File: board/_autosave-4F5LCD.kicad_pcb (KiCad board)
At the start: 2 copper layers, 58 parts, among them J101 Conn_01x10_Pin, J102 Conn_02x16_Top_Bottom, J103 Conn_02x02_Counter_Clockwise, U101 TLS850C2TEV33, U102 ESP32-S3-DEVKITC-1U-N8R2, U103 MCP2515-xSO, U104 SN65HVD230, U105 MCP2515-xSO, U106 SN65HVD230, U107 MCP2515-xSO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

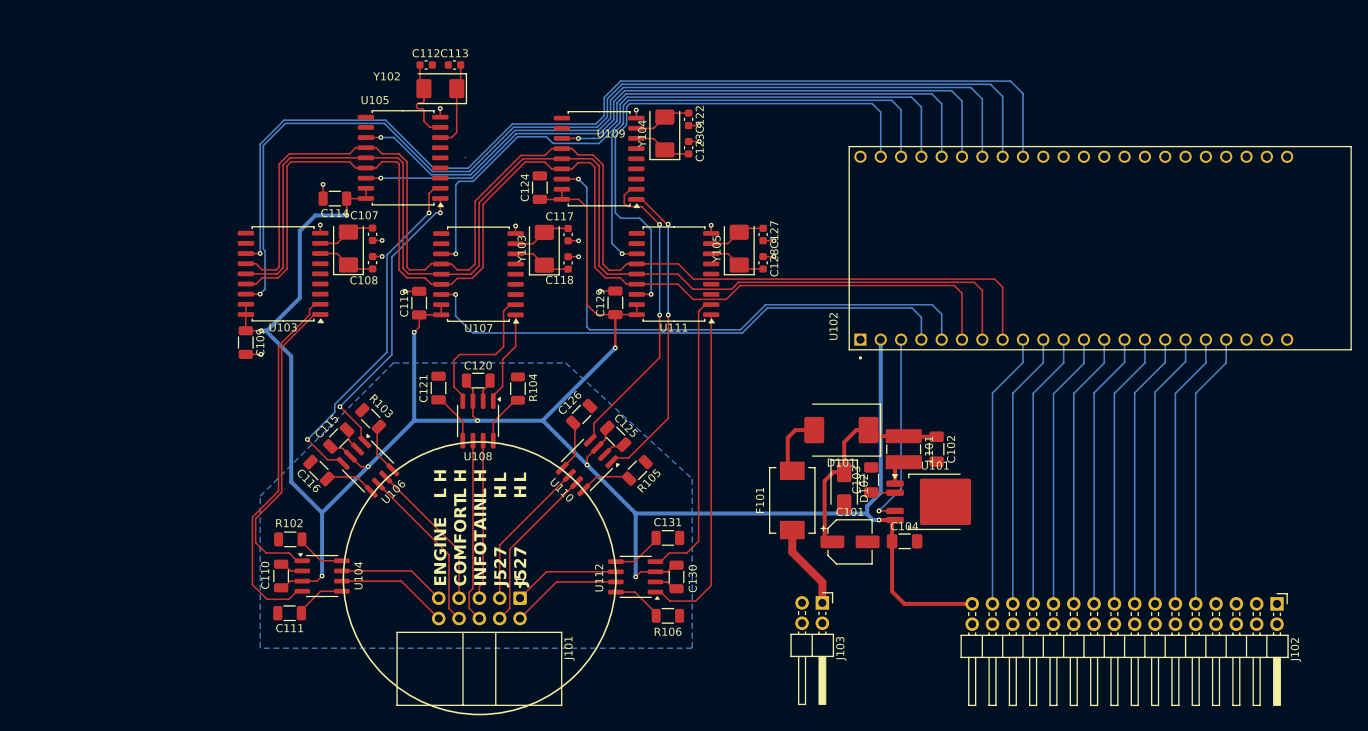
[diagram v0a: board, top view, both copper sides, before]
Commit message: Added stl and skp files for 3D printing, changed ground planes and net names, exported schematics as pdf
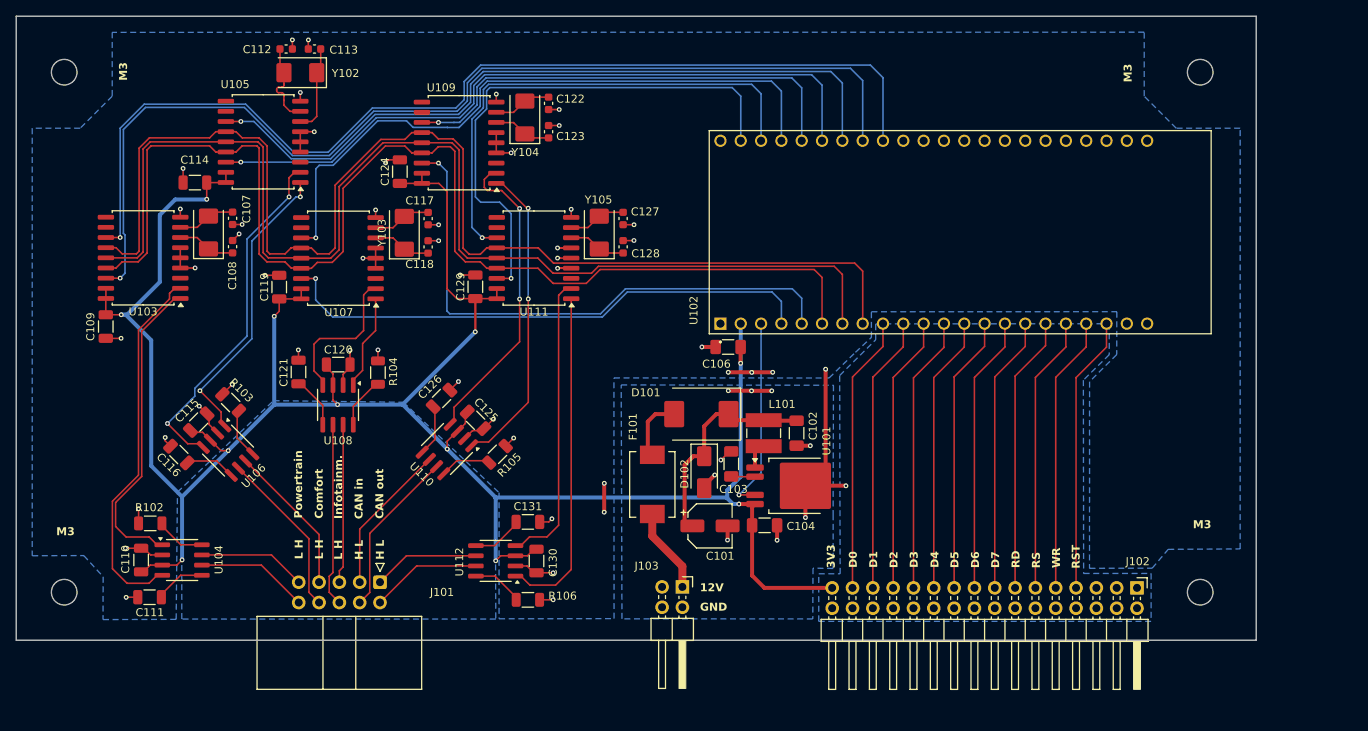
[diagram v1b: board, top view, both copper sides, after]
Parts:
- added C106: 100nF, Capacitor_SMD:C_1206_3216Metric_Pad1.33x1.80mm_HandSolder, F.Cu at (159.5, 89.3)
- added REF**: MountingHole_3.2mm_M3, MountingHole:MountingHole_3.2mm_M3, F.Cu at (76.5, 55.0)
- added REF**: MountingHole_3.2mm_M3, MountingHole:MountingHole_3.2mm_M3, F.Cu at (76.5, 120.0)
- added REF**: MountingHole_3.2mm_M3, MountingHole:MountingHole_3.2mm_M3, F.Cu at (218.5, 120.0)
- added REF**: MountingHole_3.2mm_M3, MountingHole:MountingHole_3.2mm_M3, F.Cu at (218.5, 55.0)
- J103: value Conn_02x02_Counter_Clockwise -> 02x02
- moved C117 17.6 mm to (122.0, 73.3)
- moved C118 17.6 mm to (122.0, 76.8)
- moved C124 17.6 mm to (118.5, 67.4)
- moved C126 17.6 mm to (123.7, 95.8)
- moved J101 17.6 mm to (116.0, 118.8)
- moved U108 17.6 mm to (110.7, 96.6)
- moved U109 17.6 mm to (125.9, 63.8)
- moved U110 17.6 mm to (124.3, 102.1)
- moved C123 17.6 mm to (137.0, 62.4)
- moved C101 17.6 mm to (157.2, 111.7)
- moved C102 17.6 mm to (168.1, 100.1)
- moved C103 17.6 mm to (159.9, 104.0)
- moved C104 17.6 mm to (164.1, 111.6)
- moved C107 17.6 mm to (97.5, 73.3)
- moved C108 17.6 mm to (97.5, 76.8)
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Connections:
- C101 pad 2: CAN_GND -> GND_PWR
- C102 pad 2: CAN_GND -> GND_PWR
- C103 pad 2: CAN_GND -> GND_PWR
- C104 pad 2: CAN_GND -> GND_PWR
- C107 pad 2: CAN_GND -> GND_MCU
- C108 pad 1: CAN_GND -> GND_MCU
- C109 pad 2: CAN_GND -> GND_MCU
- C110 pad 2: CAN_GND -> GND_MCU
- C111 pad 2: CAN_GND -> GND_MCU
- C112 pad 2: CAN_GND -> GND_MCU
- C113 pad 1: CAN_GND -> GND_MCU
- C114 pad 2: CAN_GND -> GND_MCU
- C115 pad 2: CAN_GND -> GND_MCU
- C116 pad 2: CAN_GND -> GND_MCU
- C117 pad 2: CAN_GND -> GND_MCU
- C118 pad 1: CAN_GND -> GND_MCU
- C119 pad 2: CAN_GND -> GND_MCU
- C120 pad 2: CAN_GND -> GND_MCU
- C121 pad 2: CAN_GND -> GND_MCU
- C122 pad 2: CAN_GND -> GND_MCU
- C123 pad 1: CAN_GND -> GND_MCU
- C124 pad 2: CAN_GND -> GND_MCU
- C125 pad 2: CAN_GND -> GND_MCU
- C126 pad 2: CAN_GND -> GND_MCU
- C127 pad 2: CAN_GND -> GND_MCU
- C128 pad 1: CAN_GND -> GND_MCU
- C129 pad 2: CAN_GND -> GND_MCU
- C130 pad 2: CAN_GND -> GND_MCU
- C131 pad 2: CAN_GND -> GND_MCU
- D102 pad 2: CAN_GND -> GND_PWR
- J102 pad 10: CAN_GND -> GND_LCD
- J102 pad 12: CAN_GND -> GND_LCD
- J102 pad 14: CAN_GND -> GND_LCD
- J102 pad 16: CAN_GND -> GND_LCD
- J102 pad 18: CAN_GND -> GND_LCD
- J102 pad 20: CAN_GND -> GND_LCD
- J102 pad 22: CAN_GND -> GND_LCD
- J102 pad 24: CAN_GND -> GND_LCD
- J102 pad 26: CAN_GND -> GND_LCD
- J102 pad 28: CAN_GND -> GND_LCD
- J102 pad 30: CAN_GND -> GND_LCD
- J102 pad 32: CAN_GND -> GND_LCD
- J102 pad 6: unconnected-(J102-Pin_6-Pad6) -> GND_LCD
- J102 pad 7: unconnected-(J102-Pin_7-Pad7) -> LCD_RST
- J102 pad 8: CAN_GND -> GND_LCD
- J103 pad 2: CAN_GND -> GND_PWR
- R102 pad 2: CAN_GND -> GND_MCU
- R103 pad 2: CAN_GND -> GND_MCU
- R104 pad 2: CAN_GND -> GND_MCU
- R105 pad 2: CAN_GND -> GND_MCU
- R106 pad 2: CAN_GND -> GND_MCU
- U101 pad 3: CAN_GND -> GND_PWR
- U102 pad J1_20: unconnected-(U102-GPIO14-PadJ1_20) -> LCD_RST
- U102 pad J1_22: CAN_GND -> GND_MCU
- U102 pad J3_1: CAN_GND -> GND_MCU
- U102 pad J3_21: CAN_GND -> GND_MCU
- U102 pad J3_22: CAN_GND -> GND_MCU
- U103 pad 4: CAN_GND -> GND_MCU
- U103 pad 5: CAN_GND -> GND_MCU
- U103 pad 6: CAN_GND -> GND_MCU
- U103 pad 9: CAN_GND -> GND_MCU
- U104 pad 2: CAN_GND -> GND_MCU
- U105 pad 4: CAN_GND -> GND_MCU
- U105 pad 5: CAN_GND -> GND_MCU
- U105 pad 6: CAN_GND -> GND_MCU
- U105 pad 9: CAN_GND -> GND_MCU
- U106 pad 2: CAN_GND -> GND_MCU
- U107 pad 4: CAN_GND -> GND_MCU
- U107 pad 5: CAN_GND -> GND_MCU
- U107 pad 6: CAN_GND -> GND_MCU
- U107 pad 9: CAN_GND -> GND_MCU
- U108 pad 2: CAN_GND -> GND_MCU
- U109 pad 4: CAN_GND -> GND_MCU
- U109 pad 5: CAN_GND -> GND_MCU
- U109 pad 6: CAN_GND -> GND_MCU
- U109 pad 9: CAN_GND -> GND_MCU
- U110 pad 2: CAN_GND -> GND_MCU
- U111 pad 4: CAN_GND -> GND_MCU
- U111 pad 5: CAN_GND -> GND_MCU
- U111 pad 6: CAN_GND -> GND_MCU
- U111 pad 9: CAN_GND -> GND_MCU
- U112 pad 2: CAN_GND -> GND_MCU
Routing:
- net GND_MCU: track 0.00 -> 101.3 mm, vias 0 -> 49
- net CAN_GND: track 37.6 -> 0.00 mm, vias 17 -> 0
- net LCD_RST: track 0.00 -> 34.6 mm
- net GND_PWR: track 0.00 -> 18.7 mm, vias 0 -> 9
- net +3.3V: track 289.2 -> 291.2 mm, vias 10 -> 11
- net GND_LCD: vias 0 -> 1
- added copper zone on B.Cu, net (none)
- added copper zone on B.Cu, net GND_LCD
- added copper zone on B.Cu, net GND_MCU
- added copper zone on B.Cu, net GND_PWR
- removed copper zone on B.Cu, net CAN_GND
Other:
- board outline added: 155 x 78 mm
- board text added: "(C) Code99 www.code99.it"
- board text added: "12V"
- board text added: "3V3"
- board text added: "4F5LCD HW 01-01-01"
- board text added: "CAN in"
- board text added: "CAN out"
- board text added: "Comfort"
- board text added: "D0"
- board text added: "D1"
- board text added: "D2"
- board text added: "D3"
- board text added: "D4"
- board text added: "D5"
- board text added: "D6"
- board text added: "D7"
- board text added: "GND"
- board text added: "GND_CAN"
- board text added: "GND_LCD"
- board text added: "GND_MCU"
- board text added: "GND_PWR"
- board text added: "H L"
- board text added: "Infotainm."
- board text added: "L H"
- board text added: "M3"
- board text added: "Powertrain"
- board text added: "RD"
- board text added: "RS"
- board text added: "RST"
- board text added: "WR"
- board text removed: "CAN_GND"
- board text removed: "COMFORT"
- board text removed: "ENGINE"
- board text removed: "H"
- board text removed: "INFOTAIN"
- board text removed: "J527"
- board text removed: "L"
